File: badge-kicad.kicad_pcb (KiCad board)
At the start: 2 copper layers, 152.7 x 76.7 mm, 126 parts, among them J2 JTAG, P2 CONN_02X20, P3 FTDI BACKUP, P4 USB_MICRO_RIGHT, P5 LED OUT (DNP), SW1 RESET, SW2 POWERON, SW3 TM1000, SW4 UP, SW5 DN, SW6 LEFT, SW7 RIGHT, SW8 ENTER, U1 WS2812B, U10 WS2812B, U11 WS2812B, U12 WS2812B, U13 MKW01Z128, U14 FT232RL SSOP, U15 MF-REG-SOT235-3.3V-300mA, U16 MCP73831T-2ACI/OT, U18 LM386, U2 WS2812B, U3 WS2812B, U4 WS2812B, U5 WS2812B, U6 WS2812B, U7 WS2812B, U8 WS2812B, U9 WS2812B, Y1 EXS00A-CS02368

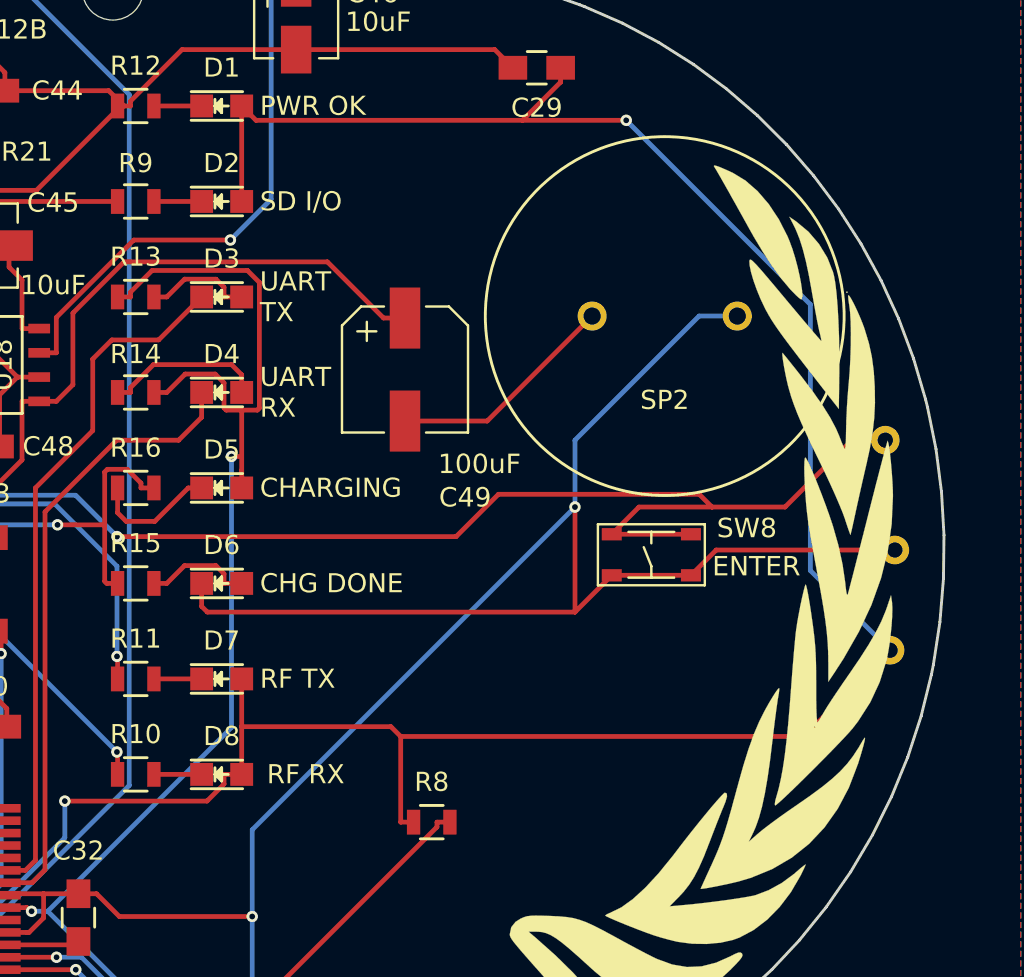
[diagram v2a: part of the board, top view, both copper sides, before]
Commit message: add silkscreens and fix some traces
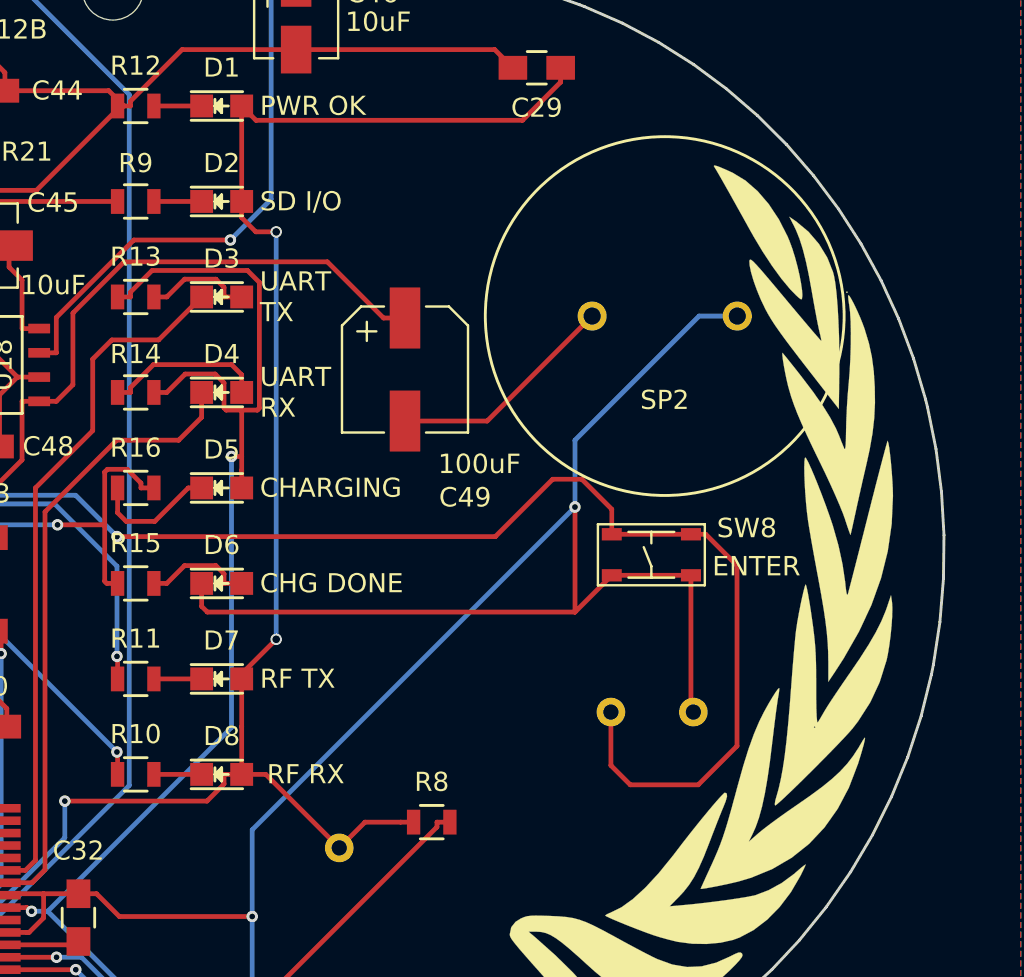
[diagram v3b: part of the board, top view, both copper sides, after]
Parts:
- moved TP9 30.6 mm to (193.7, 104.6)
- moved TP1 20.2 mm to (207.9, 97.5)
- moved TP2 13.5 mm to (212.2, 97.5)
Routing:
- net VCC: track 331.2 -> 289.4 mm, vias 5 -> 6
- net GND: track 823.6 -> 819.6 mm
- net SWENTER: track 99.8 -> 103.4 mm
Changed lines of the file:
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@@
 (kicad_pcb (version 20160815) (host pcbnew "(2016-12-18 revision 3ffa37c)-master")
   (general
-    (links 0)
+    (links 278)
     (no_connects 0)
     (area 72.606224 50.56983 225.427963 127.397751)
     (thickness 1.6)
     (drawings 361)
-    (tracks 1472)
+    (tracks 1477)
     (zones 0)
     (modules 126)
@@
   (page A4)
   (layers
-    (0 F.Cu mixed hide)
-    (31 B.Cu mixed hide)
+    (0 F.Cu mixed)
+    (31 B.Cu mixed)
     (32 B.Adhes user)
-    (33 F.Adhes user hide)
+    (33 F.Adhes user)
     (34 B.Paste user)
     (35 F.Paste user)
@@
     (38 B.Mask user)
     (39 F.Mask user)
-    (40 Dwgs.User user)
+    (40 Dwgs.User user hide)
     (41 Cmts.User user)
     (42 Eco1.User user)
@@
     (47 F.CrtYd user)
     (48 B.Fab user)
-    (49 F.Fab user)
+    (49 F.Fab user hide)
   )
   (setup
@@
   )
   (module Measurement_Points:Measurement_Point_Round-TH_Small (layer F.Cu)
-    (at 222.53 94.262)
+    (at 193.688 104.61)
     (descr "Mesurement Point, Square, Trough Hole,  DM 1.5mm, Drill 0.8mm,")
     (tags "Mesurement Point Round Trough Hole 1.5mm Drill 0.8mm")
@@
   )
   (module Measurement_Points:Measurement_Point_Round-TH_Small (layer F.Cu)
-    (at 222.28 83.262)
+    (at 207.912 97.498)
     (descr "Mesurement Point, Square, Trough Hole,  DM 1.5mm, Drill 0.8mm,")
     (tags "Mesurement Point Round Trough Hole 1.5mm Drill 0.8mm")
@@
   )
   (module Measurement_Points:Measurement_Point_Round-TH_Small (layer F.Cu)
-    (at 222.78 89.012)
+    (at 212.23 97.498)
     (descr "Mesurement Point, Square, Trough Hole,  DM 1.5mm, Drill 0.8mm,")
     (tags "Mesurement Point Round Trough Hole 1.5mm Drill 0.8mm")
@@
   (segment (start 81.28 75.012) (end 80.03 73.762) (width 0.25) (layer F.Cu) (net 6))
   (segment (start 84.53 75.012) (end 81.28 75.012) (width 0.25) (layer F.Cu) (net 6))
+  (segment (start 212.10264 90.33642) (end 212.10264 97.37064) (width 0.25) (layer F.Cu) (net 9))
+  (segment (start 212.10264 97.37064) (end 212.23 97.498) (width 0.25) (layer F.Cu) (net 9))
   (segment (start 183.93214 122.792) (end 183.93214 125.35994) (width 0.25) (layer B.Cu) (net 9))
   (segment (start 183.93214 125.35994) (end 183.83054 125.46154) (width 0.25) (layer B.Cu) (net 9))
@@
   (segment (start 174.53 103.762) (end 174.53 100.012) (width 0.25) (layer F.Cu) (net 9))
   (segment (start 212.103 90.3364) (end 212.1026 90.3364) (width 0.25) (layer F.Cu) (net 9))
-  (segment (start 213.427 89.012) (end 212.103 90.3364) (width 0.25) (layer F.Cu) (net 9))
-  (segment (start 222.78 89.012) (end 213.427 89.012) (width 0.25) (layer F.Cu) (net 9))
   (segment (start 212.1026 90.3364) (end 207.9574 90.3364) (width 0.25) (layer F.Cu) (net 9))
   (segment (start 207.957 90.3364) (end 206.032 92.262) (width 0.25) (layer F.Cu) (net 9))
@@
   (segment (start 152.3108 84.2856) (end 154.7502 84.2856) (width 0.25) (layer F.Cu) (net 16))
   (segment (start 151.6498 84.9466) (end 152.3108 84.2856) (width 0.25) (layer F.Cu) (net 16))
-  (via (at 208.7136 66.512) (size 0.6) (layers F.Cu B.Cu) (net 17))
+  (segment (start 190.386 93.688) (end 188.57902 95.49498) (width 0.25) (layer F.Cu) (net 17))
+  (segment (start 188.57902 95.49498) (end 188.57902 95.762) (width 0.25) (layer F.Cu) (net 17))
+  (segment (start 190.386 72.352) (end 190.386 93.688) (width 0.25) (layer B.Cu) (net 17))
+  (via (at 190.386 93.688) (size 0.6) (drill 0.4) (layers F.Cu B.Cu) (net 17))
+  (segment (start 188.57902 70.762) (end 188.57902 71.61144) (width 0.25) (layer F.Cu) (net 17))
+  (segment (start 188.57902 71.61144) (end 189.31958 72.352) (width 0.25) (layer F.Cu) (net 17))
+  (segment (start 189.31958 72.352) (end 190.386 72.352) (width 0.25) (layer F.Cu) (net 17))
+  (via (at 190.386 72.352) (size 0.6) (drill 0.4) (layers F.Cu B.Cu) (net 17))
+  (segment (start 188.57902 100.762) (end 189.84 100.762) (width 0.25) (layer F.Cu) (net 17))
+  (segment (start 189.84 100.762) (end 193.688 104.61) (width 0.25) (layer F.Cu) (net 17))
+  (segment (start 196.9047 103.262) (end 195.036 103.262) (width 0.25) (layer F.Cu) (net 17))
+  (segment (start 195.036 103.262) (end 193.688 104.61) (width 0.25) (layer F.Cu) (net 17))
   (via (at 132.6637 85.8259) (size 0.6) (layers F.Cu B.Cu) (net 17))
   (via (at 179.318 102.1592) (size 0.6) (layers F.Cu B.Cu) (net 17))
@@
   (segment (start 189.329 66.512) (end 188.579 65.762) (width 0.25) (layer F.Cu) (net 17))
   (segment (start 203.28 66.512) (end 189.329 66.512) (width 0.25) (layer F.Cu) (net 17))
-  (segment (start 218.3554 76.1538) (end 208.7136 66.512) (width 0.25) (layer B.Cu) (net 17))
-  (segment (start 218.3554 90.0874) (end 218.3554 76.1538) (width 0.25) (layer B.Cu) (net 17))
-  (segment (start 222.53 94.262) (end 218.3554 90.0874) (width 0.25) (layer B.Cu) (net 17))
-  (segment (start 203.28 66.512) (end 208.7136 66.512) (width 0.25) (layer F.Cu) (net 17))
   (segment (start 106.94 111.9) (end 106.94 113.0889) (width 0.25) (layer B.Cu) (net 17))
   (segment (start 151.95 110.262) (end 150.7611 110.262) (width 0.25) (layer B.Cu) (net 17))
@@
   (segment (start 145.3267 85.4751) (end 145.1751 85.6267) (width 0.25) (layer F.Cu) (net 17))
   (segment (start 145.6501 85.4751) (end 145.3267 85.4751) (width 0.25) (layer F.Cu) (net 17))
-  (segment (start 196.3912 98.262) (end 196.9047 98.7755) (width 0.25) (layer F.Cu) (net 17))
-  (segment (start 188.579 98.262) (end 196.3912 98.262) (width 0.25) (layer F.Cu) (net 17))
-  (segment (start 218.0165 98.7755) (end 222.53 94.262) (width 0.25) (layer F.Cu) (net 17))
-  (segment (start 196.9047 98.7755) (end 218.0165 98.7755) (width 0.25) (layer F.Cu) (net 17))
-  (segment (start 196.9047 98.7755) (end 196.9047 103.262) (width 0.25) (layer F.Cu) (net 17))
   (segment (start 150.7611 110.7821) (end 150.7611 110.262) (width 0.25) (layer B.Cu) (net 17))
   (segment (start 149.2838 112.2594) (end 150.7611 110.7821) (width 0.25) (layer B.Cu) (net 17))
@@
   (segment (start 126.4218 126.7785) (end 184.2756 126.7785) (width 0.25) (layer F.Cu) (net 131))
   (segment (start 125.6785 126.0352) (end 126.4218 126.7785) (width 0.25) (layer F.Cu) (net 131))
+  (segment (start 182.048 88.3101) (end 201.8599 88.3101) (width 0.25) (layer F.Cu) (net 133))
+  (segment (start 201.8599 88.3101) (end 204.864 85.306) (width 0.25) (layer F.Cu) (net 133))
+  (segment (start 204.864 85.306) (end 206.388 85.306) (width 0.25) (layer F.Cu) (net 133))
+  (segment (start 206.388 85.306) (end 207.95736 86.87536) (width 0.25) (layer F.Cu) (net 133))
+  (segment (start 207.95736 86.87536) (end 207.95736 88.18758) (width 0.25) (layer F.Cu) (net 133))
+  (segment (start 207.912 100.292) (end 208.928 101.308) (width 0.25) (layer F.Cu) (net 133))
+  (segment (start 208.928 101.308) (end 212.484 101.308) (width 0.25) (layer F.Cu) (net 133))
+  (segment (start 207.912 97.498) (end 207.912 100.292) (width 0.25) (layer F.Cu) (net 133))
+  (segment (start 214.516 99.276) (end 212.484 101.308) (width 0.25) (layer F.Cu) (net 133))
+  (segment (start 214.516 89.82643) (end 214.516 99.276) (width 0.25) (layer F.Cu) (net 133))
+  (segment (start 212.10264 88.18758) (end 212.87715 88.18758) (width 0.25) (layer F.Cu) (net 133))
+  (segment (start 212.87715 88.18758) (end 214.516 89.82643) (width 0.25) (layer F.Cu) (net 133))
   (via (at 182.048 88.3101) (size 0.6) (layers F.Cu B.Cu) (net 133))
   (via (at 143.7408 91.5075) (size 0.6) (layers F.Cu B.Cu) (net 133))
   (segment (start 212.1026 88.1876) (end 212.103 88.1876) (width 0.25) (layer F.Cu) (net 133))
   (segment (start 207.9574 88.1876) (end 212.1026 88.1876) (width 0.25) (layer F.Cu) (net 133))
-  (segment (start 217.03 86.762) (end 213.2065 86.762) (width 0.25) (layer F.Cu) (net 133))
-  (segment (start 220.53 83.262) (end 217.03 86.762) (width 0.25) (layer F.Cu) (net 133))
-  (segment (start 222.28 83.262) (end 220.53 83.262) (width 0.25) (layer F.Cu) (net 133))
   (segment (start 207.957 88.1876) (end 207.9574 88.1876) (width 0.25) (layer F.Cu) (net 133))
-  (segment (start 209.383 86.762) (end 207.957 88.1876) (width 0.25) (layer F.Cu) (net 133))
-  (segment (start 213.2065 86.762) (end 209.383 86.762) (width 0.25) (layer F.Cu) (net 133))
-  (segment (start 199.8061 88.3101) (end 182.048 88.3101) (width 0.25) (layer F.Cu) (net 133))
-  (segment (start 202.0215 86.0947) (end 199.8061 88.3101) (width 0.25) (layer F.Cu) (net 133))
-  (segment (start 212.5392 86.0947) (end 202.0215 86.0947) (width 0.25) (layer F.Cu) (net 133))
-  (segment (start 213.2065 86.762) (end 212.5392 86.0947) (width 0.25) (layer F.Cu) (net 133))
   (segment (start 143.7984 91.4499) (end 145.1751 91.4499) (width 0.25) (layer F.Cu) (net 133))
   (segment (start 143.7408 91.5075) (end 143.7984 91.4499) (width 0.25) (layer F.Cu) (net 133))

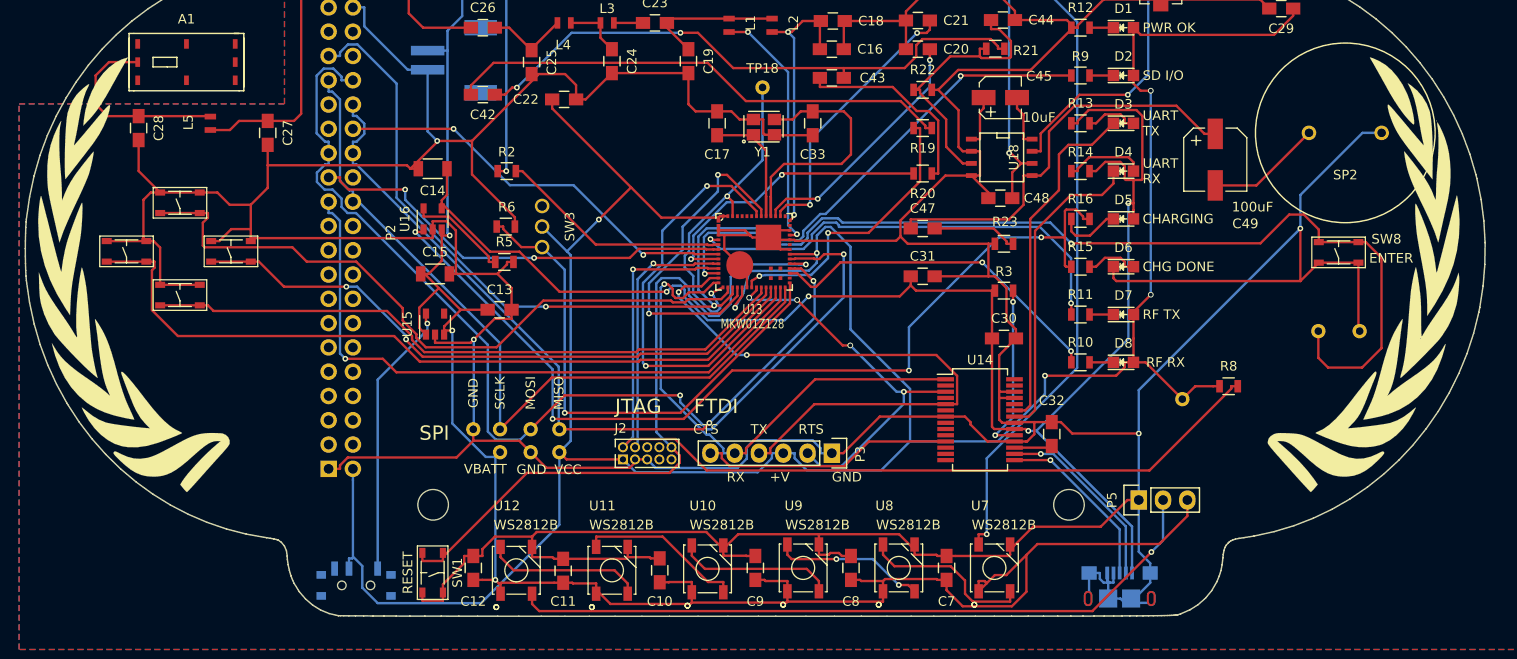
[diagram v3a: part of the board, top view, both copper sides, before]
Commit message: Fix the reset button which was tied to ground by mistake
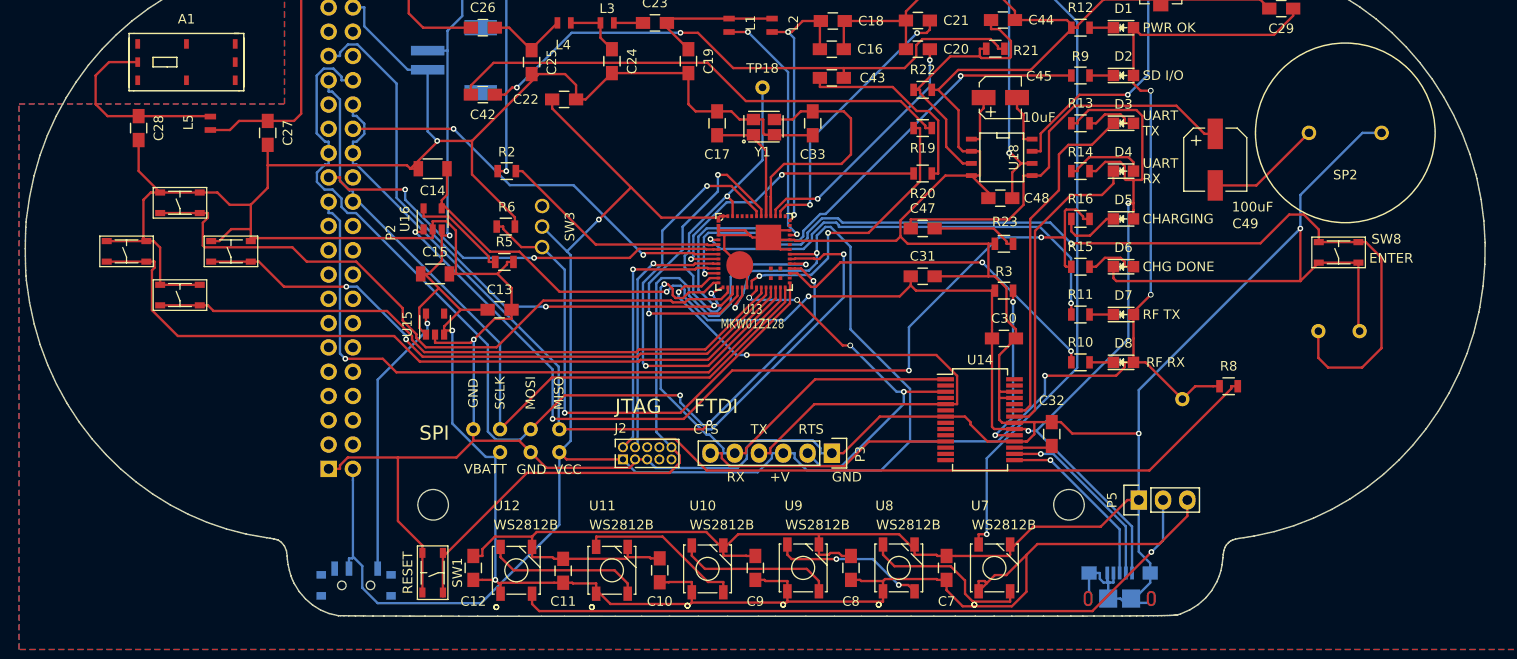
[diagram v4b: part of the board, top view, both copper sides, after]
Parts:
- removed ?: , logos:roman-head-small
- removed ?: , logos:laurel_right
- removed ?: , logos:laurel
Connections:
- SW1 pad P$2: RESET_TGTMCU -> GND
- SW1 pad P$3: GND -> RESET_TGTMCU
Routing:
- net GND: track 819.6 -> 825.3 mm
- net RESET_TGTMCU: track 76.2 -> 77.3 mm

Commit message: swap PTD7 and PTB1
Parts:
- added H7: CONN_01X01, Mounting_Holes:MountingHole_3.2mm_M3_DIN965, F.Cu at (76.3, 89.1)
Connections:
- R10 pad 1: PTD7 -> PTB1
- U13 pad 18: RF_RESET -> PTB1
- U13 pad 31: PTD7 -> RF_RESET
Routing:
- net PTB1: track 0.00 -> 61.0 mm, vias 0 -> 4
- net PTD7: track 36.1 -> 0.00 mm, vias 2 -> 0
- net GND: track 825.3 -> 820.7 mm
- net VCC: track 289.4 -> 287.2 mm
- net RF_RESET: track 35.1 -> 35.2 mm, vias 2 -> 6

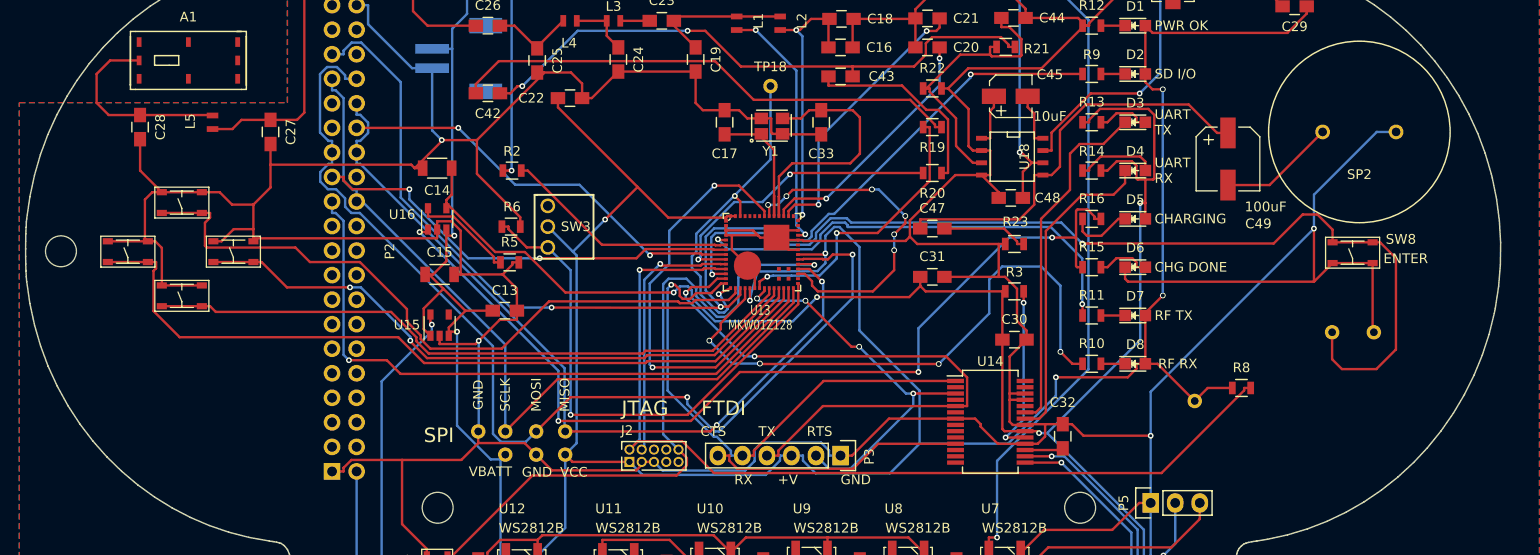
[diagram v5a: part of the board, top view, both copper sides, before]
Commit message: add text and logos to pcb
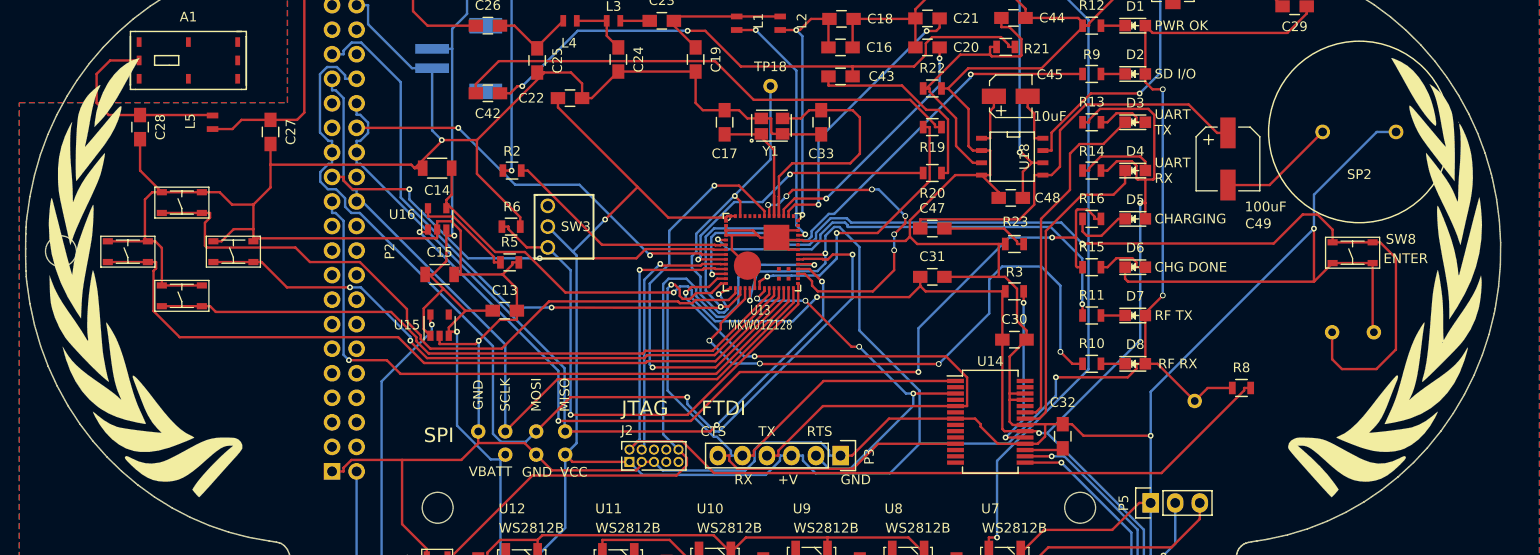
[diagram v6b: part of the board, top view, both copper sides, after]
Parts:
- added ?: , logos:laurel_right, F.Cu at (215.4, 91.7)
- added ?: , logos:laurel, F.Cu at (83.0, 91.7)
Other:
- board text added: "SPQR - The Ides of March - Revision 2 DEFCON 25 (2017) John Adams @netik (PCB, HW, SW) Bill Paul (Drivers, Board bringup, HW SW) Egan Hirvela (Game Mechanics) Matthew Harris (Art, Character Design) Based on ChbiOS RTC HAIL CASEAR! Made in San Francisco"

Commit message: Final rev2, clean up rev1
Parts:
- removed ?: , logos:laurel_right
- removed ?: , logos:laurel
- C18, C19, C23, C24, C44: footprint Capacitors_SMD:C_0805_HandSoldering -> Capacitors_SMD:C_0603_HandSoldering
